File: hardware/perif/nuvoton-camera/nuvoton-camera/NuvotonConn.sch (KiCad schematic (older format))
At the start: 6 parts, among them SW1 SW_Push, SW2 SW_Push

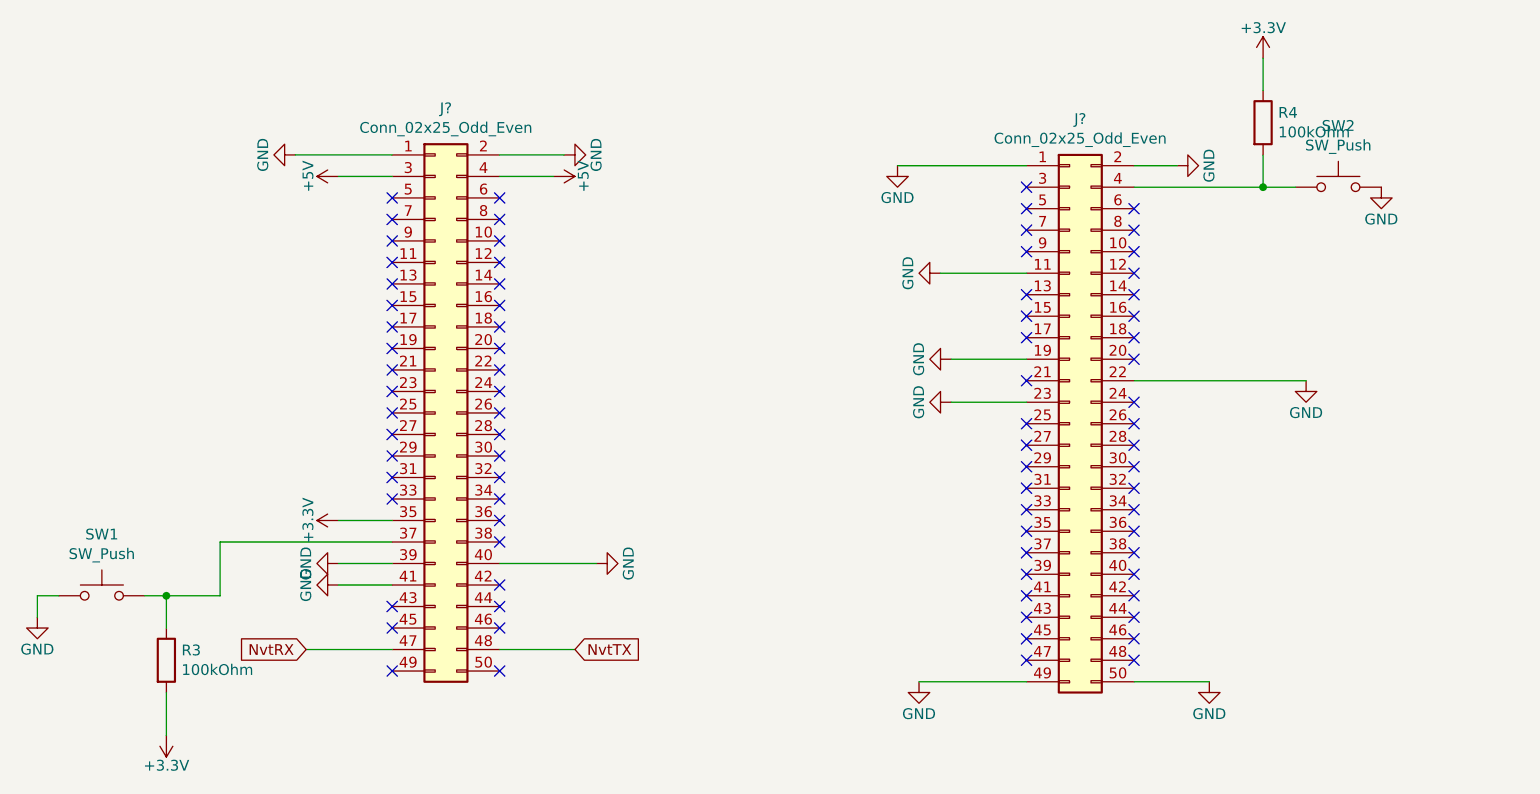
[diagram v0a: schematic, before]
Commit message: started nuvoTon N32926U1DN board skeleton
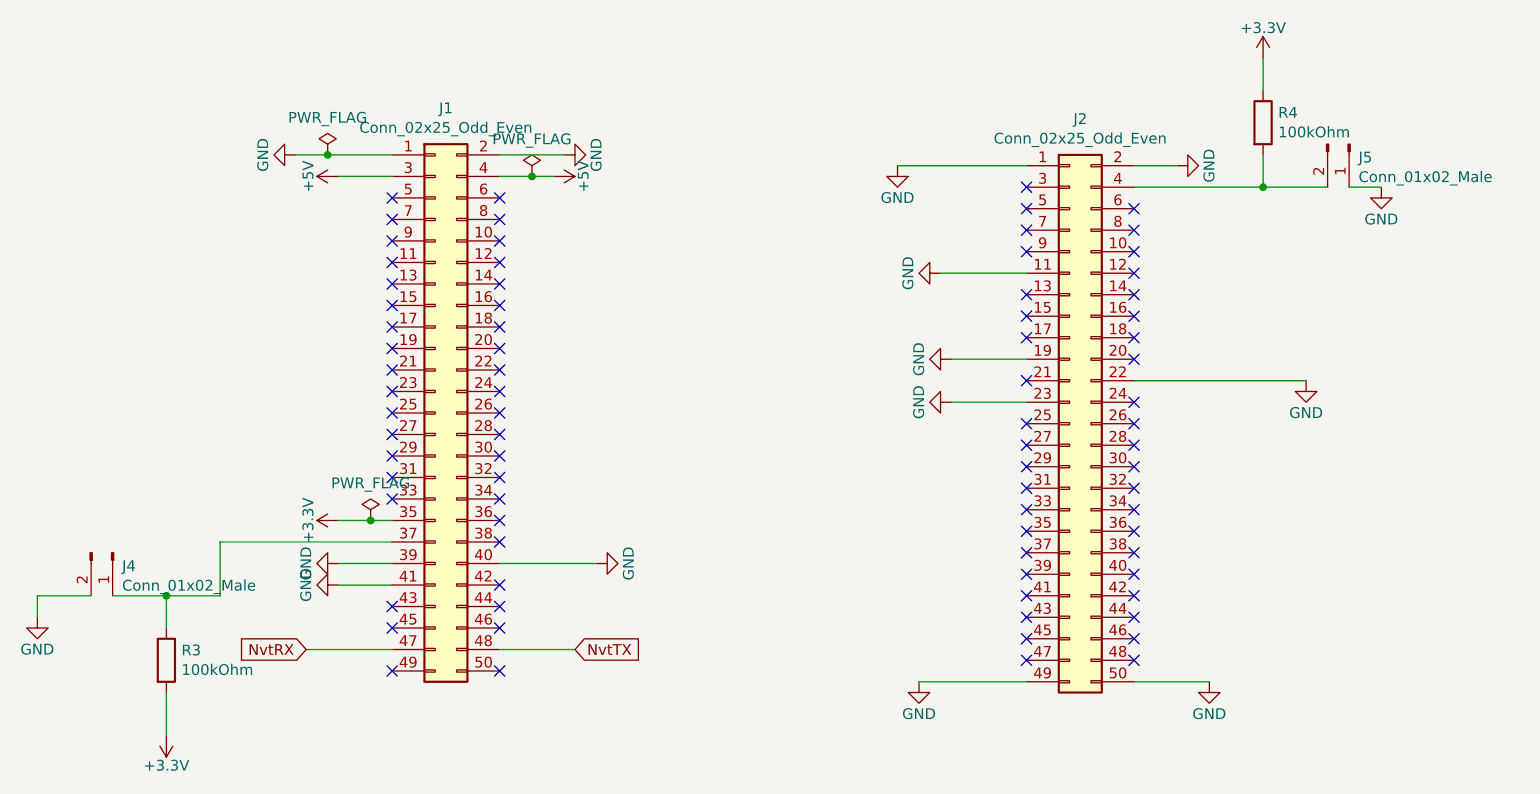
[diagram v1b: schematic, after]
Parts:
- removed SW1, SW2: SW_Push, Button_Switch_SMD:SW_SPST_TL3305C, symbol Switch:SW_Push
- added J4, J5: Conn_01x02_Male, Connector_PinSocket_2.54mm:PinSocket_1x02_P2.54mm_Vertical, symbol Connector:Conn_01x02_Male
- J1: renamed from J?; footprint (none) -> Connector_PinHeader_2.00mm:PinHeader_2x25_P2.00mm_Vertical
- J2: renamed from J?; footprint (none) -> Connector_PinSocket_2.00mm:PinSocket_2x25_P2.00mm_Vertical
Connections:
- net GND: now also J4.2 (Pin_2), J5.1 (Pin_1)
- net at J2.4 (Pin_4), R4.2: now also J5.2 (Pin_2)
- net at J1.37 (Pin_37), R3.1: now also J4.1 (Pin_1)
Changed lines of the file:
@@
 $Descr A4 11693 8268
 encoding utf-8
-Sheet 2 3
+Sheet 2 4
 Title ""
 Date ""
@@
 AR Path="/5BC77E4B" Ref="#PWR?"  Part="1"
 AR Path="/5BC77B78/5BC77E4B" Ref="#PWR0101"  Part="1"
+AR Path="/5ED3DDCD/5BC77E4B" Ref="#PWR0101"  Part="1"
 F 0 "#PWR0101" H 2950 3150 50  0001 C CNN
 F 1 "+3.3V" H 2950 3440 50  0000 C CNN
@@
 AR Path="/5BC77E51" Ref="#PWR?"  Part="1"
 AR Path="/5BC77B78/5BC77E51" Ref="#PWR0102"  Part="1"
+AR Path="/5ED3DDCD/5BC77E51" Ref="#PWR0102"  Part="1"
 F 0 "#PWR0102" H 2950 1550 50  0001 C CNN
 F 1 "+5V" H 2950 1840 50  0000 C CNN
@@
 AR Path="/5BC77E57" Ref="#PWR?"  Part="1"
 AR Path="/5BC77B78/5BC77E57" Ref="#PWR0103"  Part="1"
+AR Path="/5ED3DDCD/5BC77E57" Ref="#PWR0103"  Part="1"
 F 0 "#PWR0103" H 7800 1500 50  0001 C CNN
 F 1 "GND" H 7800 1600 50  0000 C CNN
@@
 AR Path="/5BC77E63" Ref="#PWR?"  Part="1"
 AR Path="/5BC77B78/5BC77E63" Ref="#PWR0105"  Part="1"
+AR Path="/5ED3DDCD/5BC77E63" Ref="#PWR0105"  Part="1"
 F 0 "#PWR0105" H 6850 1400 50  0001 C CNN
 F 1 "GND" H 6850 1500 50  0000 C CNN
@@
 AR Path="/5BC77E69" Ref="#PWR?"  Part="1"
 AR Path="/5BC77B78/5BC77E69" Ref="#PWR0106"  Part="1"
+AR Path="/5ED3DDCD/5BC77E69" Ref="#PWR0106"  Part="1"
 F 0 "#PWR0106" H 7250 1000 50  0001 C CNN
 F 1 "+3.3V" H 7250 1290 50  0000 C CNN
@@
 	3700 3900 4050 3900
 $Comp
-L Switch:SW_Push SW2
-U 1 1 5BFDD6DD
-P 7600 1750
-F 0 "SW2" H 7600 2035 50  0000 C CNN
-F 1 "SW_Push" H 7600 1944 50  0000 C CNN
-F 2 "Button_Switch_SMD:SW_SPST_TL3305C" H 7600 1950 50  0001 C CNN
-F 3 "" H 7600 1950 50  0001 C CNN
-	1    7600 1750
-	1    0    0    -1
-$EndComp
-$Comp
-L Switch:SW_Push SW1
-U 1 1 5BFDD739
-P 1850 3650
-F 0 "SW1" H 1850 3935 50  0000 C CNN
-F 1 "SW_Push" H 1850 3844 50  0000 C CNN
-F 2 "Button_Switch_SMD:SW_SPST_TL3305C" H 1850 3850 50  0001 C CNN
-F 3 "" H 1850 3850 50  0001 C CNN
-	1    1850 3650
-	1    0    0    -1
-$EndComp
-$Comp
 L power:GND #PWR?
 U 1 1 5BFDDF9E
@@
 AR Path="/5BFDDF9E" Ref="#PWR?"  Part="1"
 AR Path="/5BC77B78/5BFDDF9E" Ref="#PWR0104"  Part="1"
+AR Path="/5ED3DDCD/5BFDDF9E" Ref="#PWR0104"  Part="1"
 F 0 "#PWR0104" H 1550 3500 50  0001 C CNN
 F 1 "GND" H 1550 3600 50  0000 C CNN
@@
 	1550 3750 1550 3650
 Wire Wire Line
-	1550 3650 1650 3650
-Wire Wire Line
-	2050 3650 2150 3650
-Wire Wire Line
 	2400 3650 2400 3400
 $Comp
@@
 AR Path="/5BFDE540" Ref="#PWR?"  Part="1"
 AR Path="/5BC77B78/5BFDE540" Ref="#PWR0122"  Part="1"
+AR Path="/5ED3DDCD/5BFDE540" Ref="#PWR0122"  Part="1"
 F 0 "#PWR0122" H 2150 4150 50  0001 C CNN
 F 1 "+3.3V" H 2150 4440 50  0000 C CNN
@@
 	2150 4100 2150 4300
 Wire Wire Line
-	2950 3300 3200 3300
+	2950 3300 3100 3300
 $Comp
 L power:GND #PWR?
@@
 AR Path="/5BFDF298" Ref="#PWR?"  Part="1"
 AR Path="/5BC77B78/5BFDF298" Ref="#PWR0123"  Part="1"
+AR Path="/5ED3DDCD/5BFDF298" Ref="#PWR0123"  Part="1"
 F 0 "#PWR0123" H 2950 3250 50  0001 C CNN
 F 1 "GND" H 2950 3350 50  0000 C CNN
@@
 AR Path="/5BFDF2AD" Ref="#PWR?"  Part="1"
 AR Path="/5BC77B78/5BFDF2AD" Ref="#PWR0124"  Part="1"
+AR Path="/5ED3DDCD/5BFDF2AD" Ref="#PWR0124"  Part="1"
 F 0 "#PWR0124" H 4150 3250 50  0001 C CNN
 F 1 "GND" H 4150 3350 50  0000 C CNN
@@
 AR Path="/5BFDF2C2" Ref="#PWR?"  Part="1"
 AR Path="/5BC77B78/5BFDF2C2" Ref="#PWR0125"  Part="1"
+AR Path="/5ED3DDCD/5BFDF2C2" Ref="#PWR0125"  Part="1"
 F 0 "#PWR0125" H 4000 1350 50  0001 C CNN
 F 1 "GND" H 4000 1450 50  0000 C CNN
@@
 AR Path="/5BFDF2D7" Ref="#PWR?"  Part="1"
 AR Path="/5BC77B78/5BFDF2D7" Ref="#PWR0126"  Part="1"
+AR Path="/5ED3DDCD/5BFDF2D7" Ref="#PWR0126"  Part="1"
 F 0 "#PWR0126" H 2750 1350 50  0001 C CNN
 F 1 "GND" H 2750 1450 50  0000 C CNN
@@
 $EndComp
 Wire Wire Line
-	2750 1600 3200 1600
+	2750 1600 2900 1600
 Wire Wire Line
 	3700 1600 4000 1600
@@
 AR Path="/5BFDFD1F" Ref="#PWR?"  Part="1"
 AR Path="/5BC77B78/5BFDFD1F" Ref="#PWR0127"  Part="1"
+AR Path="/5ED3DDCD/5BFDFD1F" Ref="#PWR0127"  Part="1"
 F 0 "#PWR0127" H 2950 3350 50  0001 C CNN
 F 1 "GND" H 2950 3450 50  0000 C CNN
@@
 AR Path="/5BFE0A99" Ref="#PWR?"  Part="1"
 AR Path="/5BC77B78/5BFE0A99" Ref="#PWR0128"  Part="1"
+AR Path="/5ED3DDCD/5BFE0A99" Ref="#PWR0128"  Part="1"
 F 0 "#PWR0128" H 3950 1550 50  0001 C CNN
 F 1 "+5V" H 3950 1840 50  0000 C CNN
@@
 $EndComp
 Wire Wire Line
-	3700 1700 3950 1700
+	3700 1700 3850 1700
 $Comp
 L power:GND #PWR?
@@
 AR Path="/5BFE0EE4" Ref="#PWR?"  Part="1"
 AR Path="/5BC77B78/5BFE0EE4" Ref="#PWR0129"  Part="1"
+AR Path="/5ED3DDCD/5BFE0EE4" Ref="#PWR0129"  Part="1"
 F 0 "#PWR0129" H 5550 1400 50  0001 C CNN
 F 1 "GND" H 5550 1500 50  0000 C CNN
@@
 AR Path="/5BFE0EF9" Ref="#PWR?"  Part="1"
 AR Path="/5BC77B78/5BFE0EF9" Ref="#PWR0130"  Part="1"
+AR Path="/5ED3DDCD/5BFE0EF9" Ref="#PWR0130"  Part="1"
 F 0 "#PWR0130" H 5750 1900 50  0001 C CNN
 F 1 "GND" H 5750 2000 50  0000 C CNN
@@
 AR Path="/5BFE0F0E" Ref="#PWR?"  Part="1"
 AR Path="/5BC77B78/5BFE0F0E" Ref="#PWR0131"  Part="1"
+AR Path="/5ED3DDCD/5BFE0F0E" Ref="#PWR0131"  Part="1"
 F 0 "#PWR0131" H 5800 2300 50  0001 C CNN
 F 1 "GND" H 5800 2400 50  0000 C CNN
@@
 AR Path="/5BFE0F23" Ref="#PWR?"  Part="1"
 AR Path="/5BC77B78/5BFE0F23" Ref="#PWR0132"  Part="1"
+AR Path="/5ED3DDCD/5BFE0F23" Ref="#PWR0132"  Part="1"
 F 0 "#PWR0132" H 5800 2500 50  0001 C CNN
 F 1 "GND" H 5800 2600 50  0000 C CNN
@@
 AR Path="/5BFE0F38" Ref="#PWR?"  Part="1"
 AR Path="/5BC77B78/5BFE0F38" Ref="#PWR0133"  Part="1"
+AR Path="/5ED3DDCD/5BFE0F38" Ref="#PWR0133"  Part="1"
 F 0 "#PWR0133" H 5650 3800 50  0001 C CNN
 F 1 "GND" H 5650 3900 50  0000 C CNN
@@
 AR Path="/5BFE0F4D" Ref="#PWR?"  Part="1"
 AR Path="/5BC77B78/5BFE0F4D" Ref="#PWR0134"  Part="1"
+AR Path="/5ED3DDCD/5BFE0F4D" Ref="#PWR0134"  Part="1"
 F 0 "#PWR0134" H 7000 3800 50  0001 C CNN
 F 1 "GND" H 7000 3900 50  0000 C CNN
@@
 AR Path="/5BFE0F62" Ref="#PWR?"  Part="1"
 AR Path="/5BC77B78/5BFE0F62" Ref="#PWR0135"  Part="1"
+AR Path="/5ED3DDCD/5BFE0F62" Ref="#PWR0135"  Part="1"
 F 0 "#PWR0135" H 7450 2400 50  0001 C CNN
 F 1 "GND" H 7450 2500 50  0000 C CNN
@@
 Connection ~ 7250 1750
 Wire Wire Line
-	7250 1750 7400 1750
-Wire Wire Line
 	6650 2650 7450 2650
 Wire Wire Line
@@
 	5750 2150 6150 2150
 $Comp
-L Connector_Generic:Conn_02x25_Odd_Even J?
+L Connector_Generic:Conn_02x25_Odd_Even J1
 U 1 1 5ED3F356
 P 3400 2800
-F 0 "J?" H 3450 4217 50  0000 C CNN
+F 0 "J1" H 3450 4217 50  0000 C CNN
 F 1 "Conn_02x25_Odd_Even" H 3450 4126 50  0000 C CNN
-F 2 "" H 3400 2800 50  0001 C CNN
+F 2 "Connector_PinHeader_2.00mm:PinHeader_2x25_P2.00mm_Vertical" H 3400 2800 50  0001 C CNN
 F 3 "~" H 3400 2800 50  0001 C CNN
 	1    3400 2800
@@
 $EndComp
 $Comp
-L Connector_Generic:Conn_02x25_Odd_Even J?
+L Connector_Generic:Conn_02x25_Odd_Even J2
 U 1 1 5ED41126
 P 6350 2850
-F 0 "J?" H 6400 4267 50  0000 C CNN
+F 0 "J2" H 6400 4267 50  0000 C CNN
 F 1 "Conn_02x25_Odd_Even" H 6400 4176 50  0000 C CNN
-F 2 "" H 6350 2850 50  0001 C CNN
+F 2 "Connector_PinSocket_2.00mm:PinSocket_2x25_P2.00mm_Vertical" H 6350 2850 50  0001 C CNN
 F 3 "~" H 6350 2850 50  0001 C CNN
 	1    6350 2850
 	1    0    0    -1
 $EndComp
+$Comp
+L power:PWR_FLAG #FLG01
+U 1 1 5ECA95BD
+P 2900 1600
+F 0 "#FLG01" H 2900 1675 50  0001 C CNN
+F 1 "PWR_FLAG" H 2900 1773 50  0000 C CNN
+F 2 "" H 2900 1600 50  0001 C CNN
+F 3 "~" H 2900 1600 50  0001 C CNN
+	1    2900 1600
+	1    0    0    -1
+$EndComp
+Connection ~ 2900 1600
+Wire Wire Line
+	2900 1600 3200 1600
+$Comp
+L power:PWR_FLAG #FLG03
+U 1 1 5ECAB8FB
+P 3850 1700
+F 0 "#FLG03" H 3850 1775 50  0001 C CNN
+F 1 "PWR_FLAG" H 3850 1873 50  0000 C CNN
+F 2 "" H 3850 1700 50  0001 C CNN
+F 3 "~" H 3850 1700 50  0001 C CNN
+	1    3850 1700
+	1    0    0    -1
+$EndComp
+Connection ~ 3850 1700
+Wire Wire Line
+	3850 1700 3950 1700
+$Comp
+L power:PWR_FLAG #FLG02
+U 1 1 5ECABFBA
+P 3100 3300
+F 0 "#FLG02" H 3100 3375 50  0001 C CNN
+F 1 "PWR_FLAG" H 3100 3473 50  0000 C CNN
+F 2 "" H 3100 3300 50  0001 C CNN
+F 3 "~" H 3100 3300 50  0001 C CNN
+	1    3100 3300
+	1    0    0    -1
+$EndComp
+Connection ~ 3100 3300
+Wire Wire Line
+	3100 3300 3200 3300
+$Comp
+L Connector:Conn_01x02_Male J4
+U 1 1 5ECAFC08
+P 1900 3450
+F 0 "J4" V 1962 3494 50  0000 L CNN
+F 1 "Conn_01x02_Male" V 2053 3494 50  0000 L CNN
+F 2 "Connector_PinSocket_2.54mm:PinSocket_1x02_P2.54mm_Vertical" H 1900 3450 50  0001 C CNN
+F 3 "~" H 1900 3450 50  0001 C CNN
+	1    1900 3450
+	0    1    1    0
+$EndComp
+$Comp
+L Connector:Conn_01x02_Male J5
+U 1 1 5ECB070F
+P 7650 1550
+F 0 "J5" V 7712 1594 50  0000 L CNN
+F 1 "Conn_01x02_Male" V 7803 1594 50  0000 L CNN
+F 2 "Connector_PinSocket_2.54mm:PinSocket_1x02_P2.54mm_Vertical" H 7650 1550 50  0001 C CNN
+F 3 "~" H 7650 1550 50  0001 C CNN
+	1    7650 1550
+	0    1    1    0
+$EndComp
+Wire Wire Line
+	7650 1750 7800 1750
+Wire Wire Line
+	7250 1750 7550 1750
+Wire Wire Line
+	1900 3650 2150 3650
+Wire Wire Line
+	1550 3650 1800 3650
 $EndSCHEMATC
